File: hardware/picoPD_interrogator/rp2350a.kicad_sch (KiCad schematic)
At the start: 31 parts, among them SW2 SW_Push

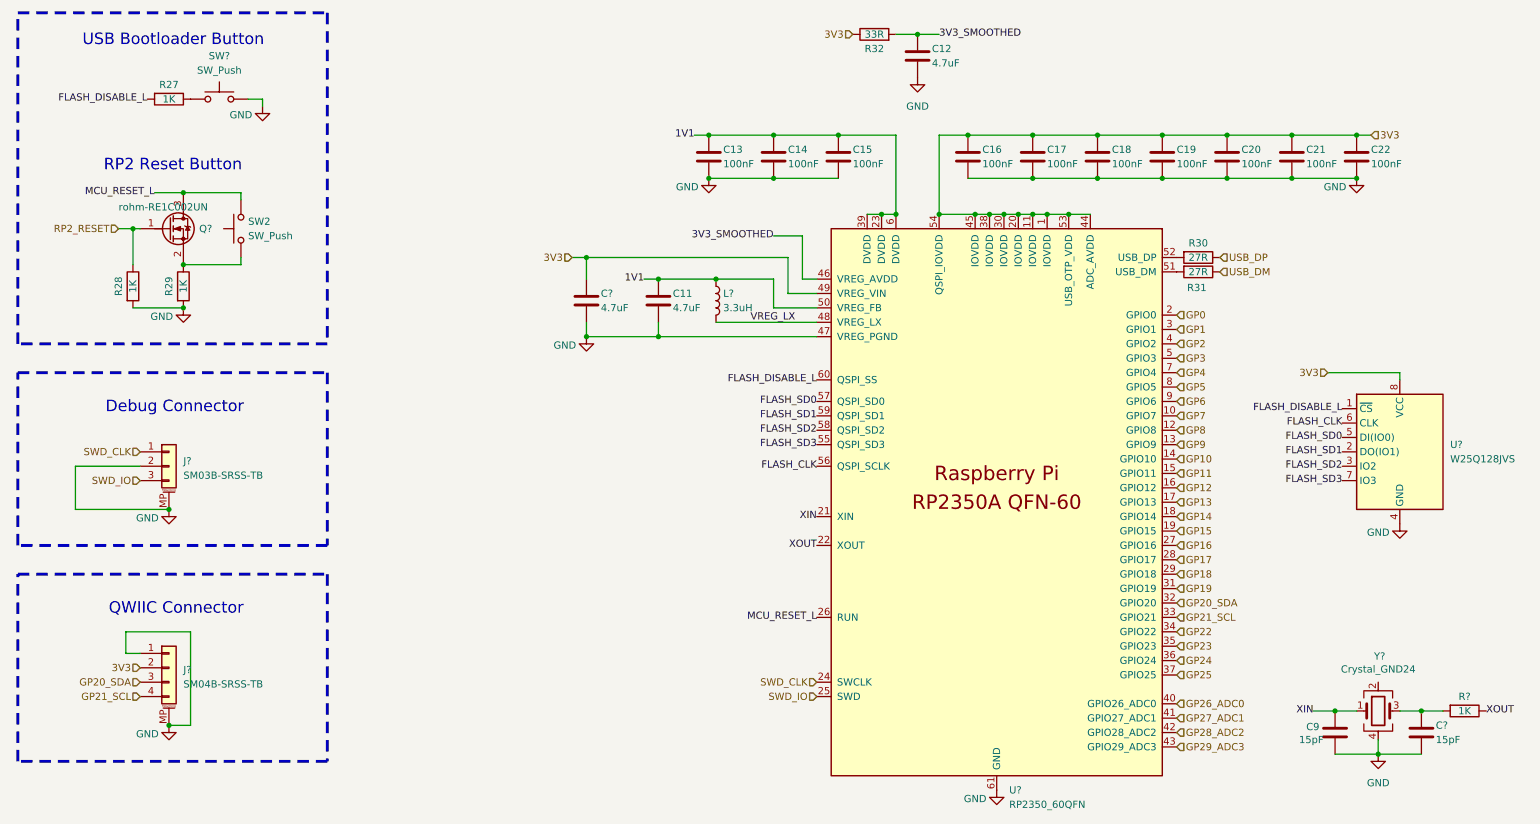
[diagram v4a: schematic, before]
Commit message: Schematic: Marked some filtering passives as DNP. Annotated schematic.
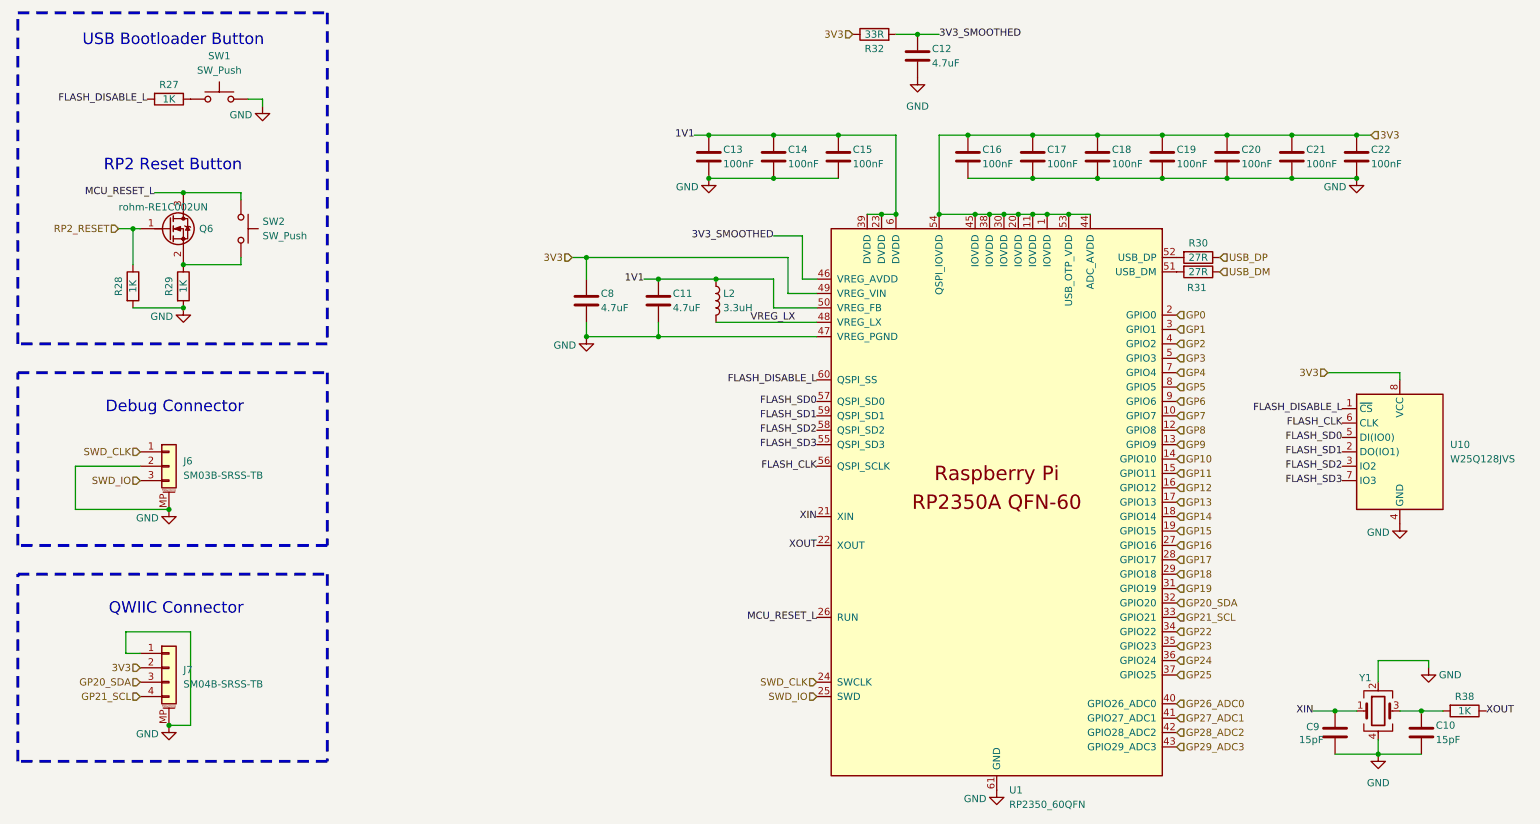
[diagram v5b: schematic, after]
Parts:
- gave numbers to parts that had none: 11
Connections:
- net GND: now also Y1.2
- net MCU_RESET_L: now also SW2.1; no longer SW2.2
- net at Q6.2 (S), R29.1: now also SW2.2; no longer SW2.1
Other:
- moved on the sheet: SW2
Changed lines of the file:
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@@
 	(wire
 		(pts
+			(xy 265.43 130.81) (xy 256.54 130.81)
+		)
+		(stroke
+			(width 0)
+			(type default)
+		)
+	)
+	(wire
+		(pts
 			(xy 179.07 38.1) (xy 184.15 38.1)
 		)
@@
 	(wire
 		(pts
+			(xy 256.54 130.81) (xy 256.54 134.62)
+		)
+		(stroke
+			(width 0)
+			(type default)
+		)
+	)
+	(wire
+		(pts
 			(xy 26.67 96.52) (xy 38.1 96.52)
 		)
@@
 	(wire
 		(pts
+			(xy 265.43 132.08) (xy 265.43 130.81)
+		)
+		(stroke
+			(width 0)
+			(type default)
+		)
+	)
+	(wire
+		(pts
 			(xy 193.04 52.07) (xy 195.58 52.07)
 		)
@@
 		(dnp no)
 		(fields_autoplaced yes)
-		(property "Reference" "U?"
+		(property "Reference" "U1"
 			(at 191.4241 153.67 0)
 			(effects
@@
 			(project "picoPD_interrogator"
 				(path "/e34b0978-7def-4921-94d0-accc0a677529/dcdf1db7-f9f6-495b-a623-7e4b73e77f06"
-					(reference "U?")
+					(reference "U1")
 					(unit 1)
 				)
@@
 		(dnp no)
 		(fields_autoplaced yes)
-		(property "Reference" "U?"
+		(property "Reference" "U10"
 			(at 269.24 92.7099 0)
 			(effects
@@
 			(project "picoPD_interrogator"
 				(path "/e34b0978-7def-4921-94d0-accc0a677529/dcdf1db7-f9f6-495b-a623-7e4b73e77f06"
-					(reference "U?")
+					(reference "U10")
 					(unit 1)
 				)
@@
 		(on_board yes)
 		(dnp no)
-		(property "Reference" "Y?"
-			(at 256.794 130.048 0)
+		(property "Reference" "Y1"
+			(at 254.254 133.858 0)
 			(effects
 				(font
@@
 		)
 		(property "Value" "Crystal_GND24"
-			(at 256.54 132.334 0)
+			(at 247.65 133.604 0)
 			(effects
 				(font
 					(size 1.27 1.27)
 				)
+				(hide yes)
 			)
 		)
@@
 			(project "picoPD_interrogator"
 				(path "/e34b0978-7def-4921-94d0-accc0a677529/dcdf1db7-f9f6-495b-a623-7e4b73e77f06"
-					(reference "Y?")
+					(reference "Y1")
 					(unit 1)
 				)
@@
 		(dnp no)
 		(fields_autoplaced yes)
-		(property "Reference" "#PWR?"
+		(property "Reference" "#PWR0102"
 			(at 175.26 34.29 0)
 			(effects
@@
 			(project "picoPD_interrogator"
 				(path "/e34b0978-7def-4921-94d0-accc0a677529/dcdf1db7-f9f6-495b-a623-7e4b73e77f06"
-					(reference "#PWR?")
+					(reference "#PWR0102")
 					(unit 1)
 				)
@@
 		(dnp no)
 		(fields_autoplaced yes)
-		(property "Reference" "#PWR?"
+		(property "Reference" "#PWR0103"
 			(at 256.54 153.67 0)
 			(effects
@@
 			(project "picoPD_interrogator"
 				(path "/e34b0978-7def-4921-94d0-accc0a677529/dcdf1db7-f9f6-495b-a623-7e4b73e77f06"
-					(reference "#PWR?")
+					(reference "#PWR0103")
 					(unit 1)
 				)
@@
 		(dnp no)
 		(fields_autoplaced yes)
-		(property "Reference" "SW?"
+		(property "Reference" "SW1"
 			(at 52.07 24.13 0)
 			(effects
@@
 			(project "picoPD_interrogator"
 				(path "/e34b0978-7def-4921-94d0-accc0a677529/dcdf1db7-f9f6-495b-a623-7e4b73e77f06"
-					(reference "SW?")
+					(reference "SW1")
 					(unit 1)
 				)
@@
 		(dnp no)
 		(fields_autoplaced yes)
-		(property "Reference" "J?"
+		(property "Reference" "J6"
 			(at 45.72 95.6055 0)
 			(effects
@@
 			(project "picoPD_interrogator"
 				(path "/e34b0978-7def-4921-94d0-accc0a677529/dcdf1db7-f9f6-495b-a623-7e4b73e77f06"
-					(reference "J?")
+					(reference "J6")
 					(unit 1)
 				)
@@
 		(on_board yes)
 		(dnp no)
-		(property "Reference" "#PWR?"
+		(property "Reference" "#PWR0101"
 			(at 59.69 39.37 0)
 			(effects
@@
 			(project "picoPD_interrogator"
 				(path "/e34b0978-7def-4921-94d0-accc0a677529/dcdf1db7-f9f6-495b-a623-7e4b73e77f06"
-					(reference "#PWR?")
+					(reference "#PWR0101")
 					(unit 1)
 				)
@@
 		(on_board yes)
 		(dnp no)
-		(property "Reference" "C?"
+		(property "Reference" "C10"
 			(at 266.7 142.24 0)
 			(effects
@@
 			(project "picoPD_interrogator"
 				(path "/e34b0978-7def-4921-94d0-accc0a677529/dcdf1db7-f9f6-495b-a623-7e4b73e77f06"
-					(reference "C?")
+					(reference "C10")
 					(unit 1)
 				)
@@
 		(on_board yes)
 		(dnp no)
-		(property "Reference" "Q?"
+		(property "Reference" "Q6"
 			(at 48.514 54.61 0)
 			(effects
@@
 			(project "picoPD_interrogator"
 				(path "/e34b0978-7def-4921-94d0-accc0a677529/dcdf1db7-f9f6-495b-a623-7e4b73e77f06"
-					(reference "Q?")
+					(reference "Q6")
 					(unit 1)
 				)
@@
 		(on_board yes)
 		(dnp no)
-		(property "Reference" "R?"
+		(property "Reference" "R38"
 			(at 271.78 137.16 90)
 			(effects
@@
 			(project "picoPD_interrogator"
 				(path "/e34b0978-7def-4921-94d0-accc0a677529/dcdf1db7-f9f6-495b-a623-7e4b73e77f06"
-					(reference "R?")
+					(reference "R38")
 					(unit 1)
 				)
@@
 	(symbol
 		(lib_id "Switch:SW_Push")
-		(at 55.88 54.61 90)
+		(at 55.88 54.61 270)
 		(unit 1)
 		(exclude_from_sim no)
@@
 		(fields_autoplaced yes)
 		(property "Reference" "SW2"
-			(at 57.15 53.3399 90)
+			(at 59.69 53.3399 90)
 			(effects
 				(font
 					(size 1.27 1.27)
 				)
-				(justify right)
+				(justify left)
 			)
 		)
 		(property "Value" "SW_Push"
-			(at 57.15 55.8799 90)
+			(at 59.69 55.8799 90)
 			(effects
 				(font
 					(size 1.27 1.27)
 				)
-				(justify right)
+				(justify left)
 			)
 		)
 		(property "Footprint" ""
-			(at 50.8 54.61 0)
+			(at 60.96 54.61 0)
 			(effects
 				(font
@@
 		)
 		(property "Datasheet" "~"
-			(at 50.8 54.61 0)
+			(at 60.96 54.61 0)
 			(effects
 				(font
@@
 	)
 	(symbol
+		(lib_id "power:GND")
+		(at 265.43 132.08 0)
+		(unit 1)
+		(exclude_from_sim no)
+		(in_bom yes)
+		(on_board yes)
+		(dnp no)
+		(property "Reference" "#PWR012"
+			(at 265.43 138.43 0)
+			(effects
+				(font
+					(size 1.27 1.27)
+				)
+				(hide yes)
+			)
+		)
+		(property "Value" "GND"
+			(at 269.24 133.35 0)
+			(effects
+				(font
+					(size 1.27 1.27)
+				)
+			)
+		)
+		(property "Footprint" ""
+			(at 265.43 132.08 0)
+			(effects
+				(font
+					(size 1.27 1.27)
+				)
+				(hide yes)
+			)
+		)
+		(property "Datasheet" ""
+			(at 265.43 132.08 0)
+			(effects
+				(font
+					(size 1.27 1.27)
+				)
+				(hide yes)
+			)
+		)
+		(property "Description" "Power symbol creates a global label with name \"GND\" , ground"
+			(at 265.43 132.08 0)
+			(effects
+				(font
+					(size 1.27 1.27)
+				)
+				(hide yes)
+			)
+		)
+		(pin "1"
+		)
+		(instances
+			(project "picoPD_interrogator"
+				(path "/e34b0978-7def-4921-94d0-accc0a677529/dcdf1db7-f9f6-495b-a623-7e4b73e77f06"
+					(reference "#PWR012")
+					(unit 1)
+				)
+			)
+		)
+	)
+	(symbol
 		(lib_id "Device:C")
 		(at 149.86 41.91 0)
@@
 		(dnp no)
 		(fields_autoplaced yes)
-		(property "Reference" "L?"
+		(property "Reference" "L2"
 			(at 140.97 66.0399 0)
 			(effects
@@
 			(project "picoPD_interrogator"
 				(path "/e34b0978-7def-4921-94d0-accc0a677529/dcdf1db7-f9f6-495b-a623-7e4b73e77f06"
-					(reference "L?")
+					(reference "L2")
 					(unit 1)
 				)
@@
 		(on_board yes)
 		(dnp no)
-		(property "Reference" "C?"
+		(property "Reference" "C8"
 			(at 119.38 66.04 0)
 			(effects
@@
 			(project "picoPD_interrogator"
 				(path "/e34b0978-7def-4921-94d0-accc0a677529/dcdf1db7-f9f6-495b-a623-7e4b73e77f06"
-					(reference "C?")
+					(reference "C8")
 					(unit 1)
 				)
@@
 		(dnp no)
 		(fields_autoplaced yes)
-		(property "Reference" "J?"
+		(property "Reference" "J7"
 			(at 45.72 132.4355 0)
 			(effects
@@
 			(project "picoPD_interrogator"
 				(path "/e34b0978-7def-4921-94d0-accc0a677529/dcdf1db7-f9f6-495b-a623-7e4b73e77f06"
-					(reference "J?")
+					(reference "J7")
 					(unit 1)
 				)

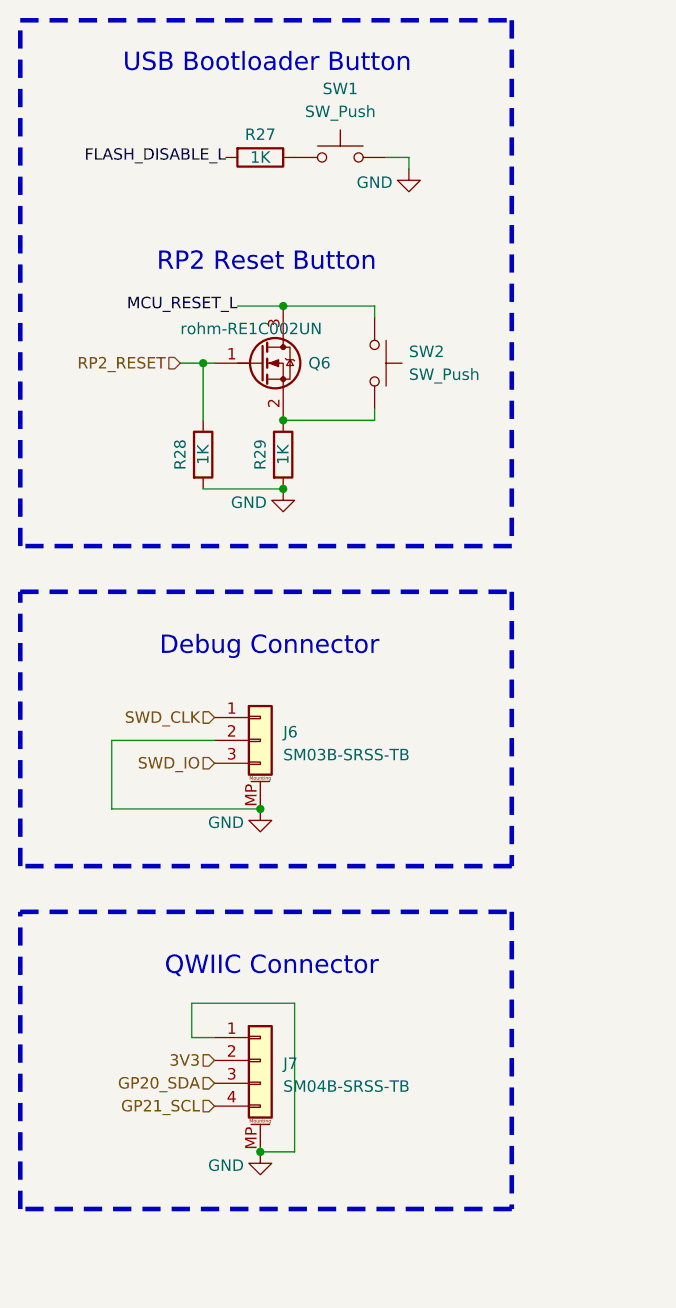
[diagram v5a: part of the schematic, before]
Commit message: Schematic/PCB: Changed the reset circuit & the reset circuit PCB layout.
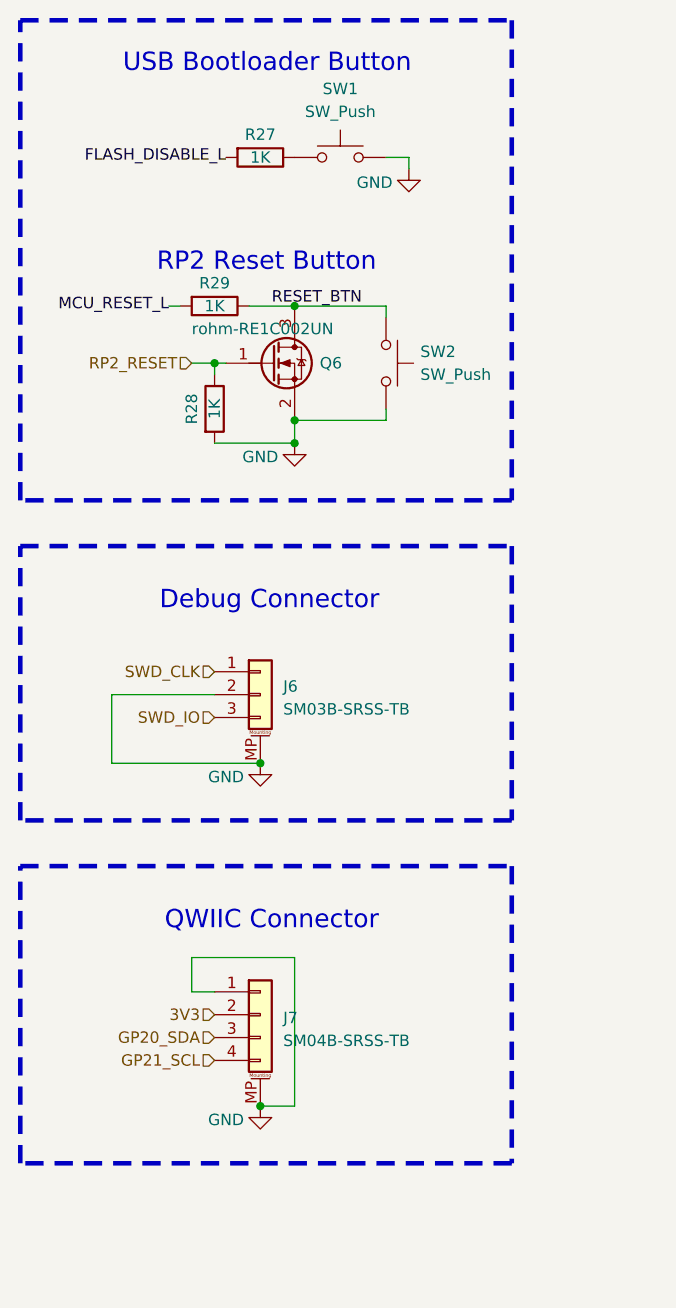
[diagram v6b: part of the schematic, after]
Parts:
- SW1, SW2: footprint (none) -> picoPD_interrogator:CK_PTS815
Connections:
- net GND: now also Q6.2 (S), SW2.2; no longer R29.2
- net MCU_RESET_L: now also R29.2; no longer Q6.3 (D), SW2.1
- new net RESET_BTN: Q6.3 (D), R29.1, SW2.1
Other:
- moved on the sheet: J6, J7, Q6, R28, R29, SW2

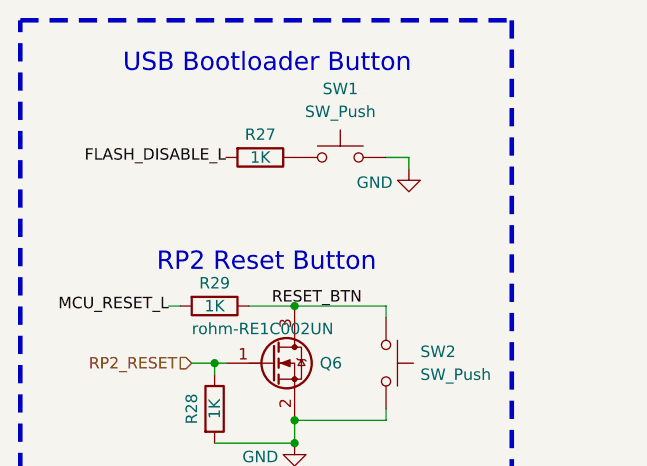
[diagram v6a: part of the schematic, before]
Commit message: PCB: Working on CC/VCONN mode/orientation/passthrough switches.
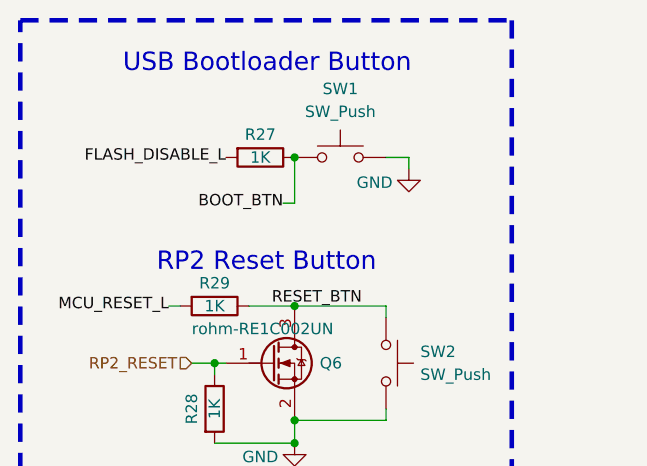
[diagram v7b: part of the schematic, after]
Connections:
- net BOOT_BTN: now reaches R27.1, SW1.1
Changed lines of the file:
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@@
+	)
+	(junction
+		(at 46.99 31.75)
+		(diameter 0)
+		(color 0 0 0 0)
 	)
 	(junction
@@
 	(wire
 		(pts
+			(xy 45.72 36.83) (xy 46.99 36.83)
+		)
+		(stroke
+			(width 0)
+			(type default)
+		)
+	)
+	(wire
+		(pts
 			(xy 187.96 52.07) (xy 190.5 52.07)
 		)
@@
 		(pts
 			(xy 264.16 139.7) (xy 267.97 139.7)
+		)
+		(stroke
+			(width 0)
+			(type default)
+		)
+	)
+	(wire
+		(pts
+			(xy 46.99 31.75) (xy 46.99 36.83)
 		)
 		(stroke
@@
 		)
 	)
+	(label "BOOT_BTN"
+		(at 45.72 36.83 180)
+		(fields_autoplaced yes)
+		(effects
+			(font
+				(size 1.27 1.27)
+			)
+			(justify right)
+		)
+	)
